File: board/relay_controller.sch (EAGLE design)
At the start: 76 parts, among them IC1 STM32F103C8T, IC3 AT24C, K1 G6K-2F-Y, K2 G6K-2F-Y, K3 G6K-2F-Y, K7 G6K-2F-Y, K8 G6K-2F-Y, Q1 220mA/50V/3.5Ω, Q2 220mA/50V/3.5Ω, Q3 220mA/50V/3.5Ω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

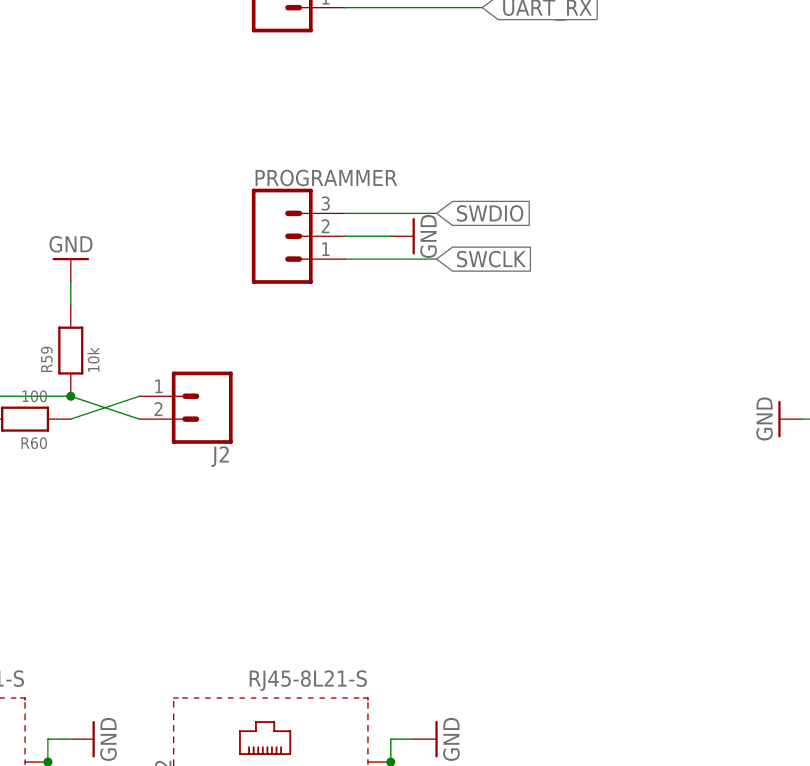
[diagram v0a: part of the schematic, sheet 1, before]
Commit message: add 3.3v to swd connector
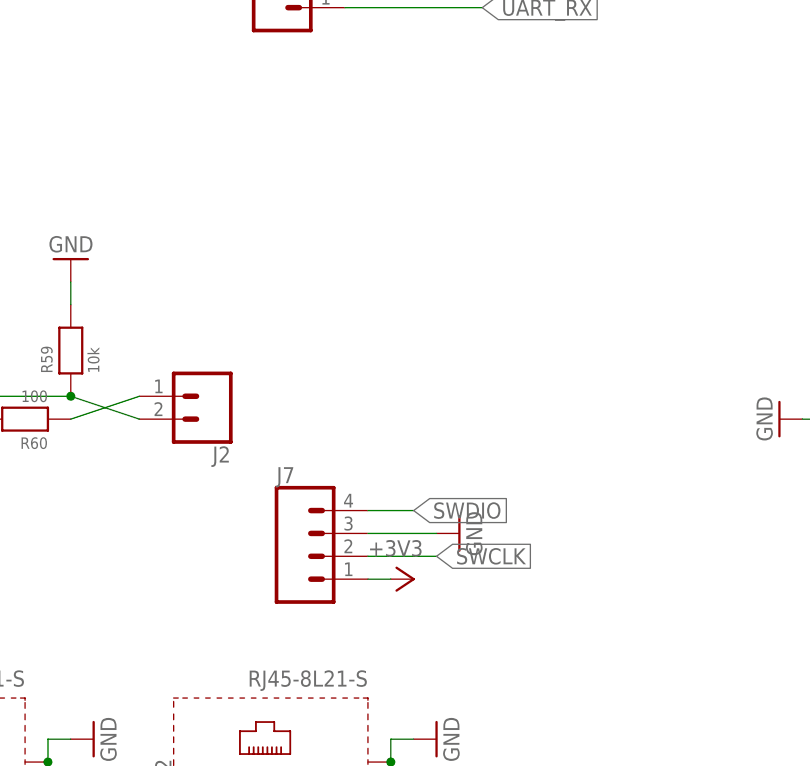
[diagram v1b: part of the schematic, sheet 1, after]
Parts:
- removed PROGRAMMER: (no value), SparkFun-Connectors:CONN_03LOCK
- added J7: (no value), SparkFun-Connectors:CONN_04POLAR_LOCK
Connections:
- net +3V3: now also J7.1
- net GND: now also J7.3; no longer PROGRAMMER.2
- net SWCLK: now also J7.2; no longer PROGRAMMER.1
- net SWDIO: now also J7.4; no longer PROGRAMMER.3
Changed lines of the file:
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@@
 <part name="GND10" library="supply1" deviceset="GND" device=""/>
 <part name="GND11" library="supply1" deviceset="GND" device=""/>
-<part name="PROGRAMMER" library="SparkFun-Connectors" deviceset="CONN_03" device="LOCK"/>
 <part name="R1" library="microbuilder" deviceset="RESISTOR" device="0603" value="10k"/>
 <part name="+3V5" library="supply1" deviceset="+3V3" device=""/>
-<part name="GND13" library="supply1" deviceset="GND" device=""/>
 <part name="GND40" library="supply1" deviceset="GND" device=""/>
 <part name="S1" library="SparkFun-Switches" deviceset="MOMENTARY-SWITCH-SPST-2" device="-SMD-4.6X2.8MM"/>
@@
 <part name="C10" library="microbuilder" deviceset="CAP_CERAMIC" device="0603" value="33pf"/>
 <part name="C2" library="microbuilder" deviceset="CAP_CERAMIC" device="0603" value="10nF"/>
+<part name="+3V11" library="supply1" deviceset="+3V3" device=""/>
+<part name="GND6" library="supply1" deviceset="GND" device=""/>
+<part name="J7" library="SparkFun-Connectors" deviceset="CONN_04" device="POLAR_LOCK"/>
 </parts>
 <sheets>
@@
 <instance part="GND10" gate="1" x="-66.04" y="66.04" rot="R270"/>
 <instance part="GND11" gate="1" x="-66.04" y="60.96" rot="R270"/>
-<instance part="PROGRAMMER" gate="J$1" x="-160.02" y="83.82"/>
 <instance part="R1" gate="G$1" x="-81.28" y="53.34"/>
 <instance part="+3V5" gate="G$1" x="-91.44" y="53.34" rot="R90"/>
-<instance part="GND13" gate="1" x="-144.78" y="83.82" rot="R90"/>
 <instance part="GND40" gate="1" x="-104.14" y="63.5" rot="R270"/>
 <instance part="S1" gate="G$1" x="-93.98" y="66.04"/>
@@
 <instance part="C10" gate="G$1" x="-55.88" y="60.96" rot="R90"/>
 <instance part="C2" gate="G$1" x="-198.12" y="71.12"/>
+<instance part="+3V11" gate="G$1" x="-144.78" y="45.72" rot="R270"/>
+<instance part="GND6" gate="1" x="-139.7" y="50.8" rot="R90"/>
+<instance part="J7" gate="G$1" x="-154.94" y="48.26"/>
 </instances>
 <busses>
@@
 </segment>
 <segment>
-<pinref part="PROGRAMMER" gate="J$1" pin="2"/>
-<pinref part="GND13" gate="1" pin="GND"/>
-<wire x1="-147.32" y1="83.82" x2="-152.4" y2="83.82" width="0.1524" layer="91"/>
-</segment>
-<segment>
 <pinref part="R5" gate="G$1" pin="1"/>
 <pinref part="GND4" gate="1" pin="GND"/>
@@
 <wire x1="-147.32" y1="27.94" x2="-144.78" y2="27.94" width="0.1524" layer="91"/>
 <pinref part="GND100" gate="1" pin="GND"/>
+</segment>
+<segment>
+<pinref part="GND6" gate="1" pin="GND"/>
+<wire x1="-142.24" y1="50.8" x2="-149.86" y2="50.8" width="0.1524" layer="91"/>
+<pinref part="J7" gate="G$1" pin="3"/>
 </segment>
 </net>
@@
 <pinref part="+3V34" gate="G$1" pin="+3V3"/>
 </segment>
+<segment>
+<pinref part="+3V11" gate="G$1" pin="+3V3"/>
+<wire x1="-147.32" y1="45.72" x2="-149.86" y2="45.72" width="0.1524" layer="91"/>
+<pinref part="J7" gate="G$1" pin="1"/>
+</segment>
 </net>
 <net name="RELAY_16" class="0">
@@
 <net name="SWDIO" class="0">
 <segment>
-<pinref part="PROGRAMMER" gate="J$1" pin="3"/>
-<wire x1="-152.4" y1="86.36" x2="-142.24" y2="86.36" width="0.1524" layer="91"/>
-<label x="-142.24" y="86.36" size="1.778" layer="95" xref="yes"/>
-</segment>
-<segment>
 <pinref part="IC1" gate="MCU" pin="PA13"/>
 <wire x1="0" y1="73.66" x2="10.16" y2="73.66" width="0.1524" layer="91"/>
 <label x="10.16" y="73.66" size="1.778" layer="95" xref="yes"/>
 </segment>
+<segment>
+<wire x1="-149.86" y1="53.34" x2="-144.78" y2="53.34" width="0.1524" layer="91"/>
+<label x="-144.78" y="53.34" size="1.778" layer="95" xref="yes"/>
+<pinref part="J7" gate="G$1" pin="4"/>
+</segment>
 </net>
 <net name="SWCLK" class="0">
-<segment>
-<label x="-142.24" y="81.28" size="1.778" layer="95" xref="yes"/>
-<pinref part="PROGRAMMER" gate="J$1" pin="1"/>
-<wire x1="-152.4" y1="81.28" x2="-142.24" y2="81.28" width="0.1524" layer="91"/>
-</segment>
 <segment>
 <pinref part="IC1" gate="MCU" pin="PA14"/>
@@
 <label x="17.78" y="76.2" size="1.778" layer="95" xref="yes"/>
 </segment>
-</net>
+<segment>
+<wire x1="-149.86" y1="48.26" x2="-142.24" y2="48.26" width="0.1524" layer="91"/>
+<label x="-142.24" y="48.26" size="1.778" layer="95" xref="yes"/>
+<pinref part="J7" gate="G$1" pin="2"/>
+</segment>
+</net>
